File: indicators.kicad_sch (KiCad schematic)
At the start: 0 parts

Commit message: Added todo list
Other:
- note added: "TODO list: - RGB LED with PWM for status indication - LED indicators for each thing: (STM LED, 3.3V power LED, USB LED, SERVO LED, 12V LED, etc. - Add Buzzer too"
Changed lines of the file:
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@@
 	(generator_version "9.0")
 	(paper "A4")
+	(text "TODO list:\n- RGB LED with PWM for status indication\n- LED indicators for each thing: (STM LED, 3.3V power LED, USB LED, SERVO LED, 12V LED, etc.\n- Add Buzzer too"
+		(exclude_from_sim no)
+		(at 145.796 99.822 0)
+		(effects
+			(font
+				(size 2.54 2.54)
+				(thickness 0.508)
+				(bold yes)
+			)
+		)
+	)
 )

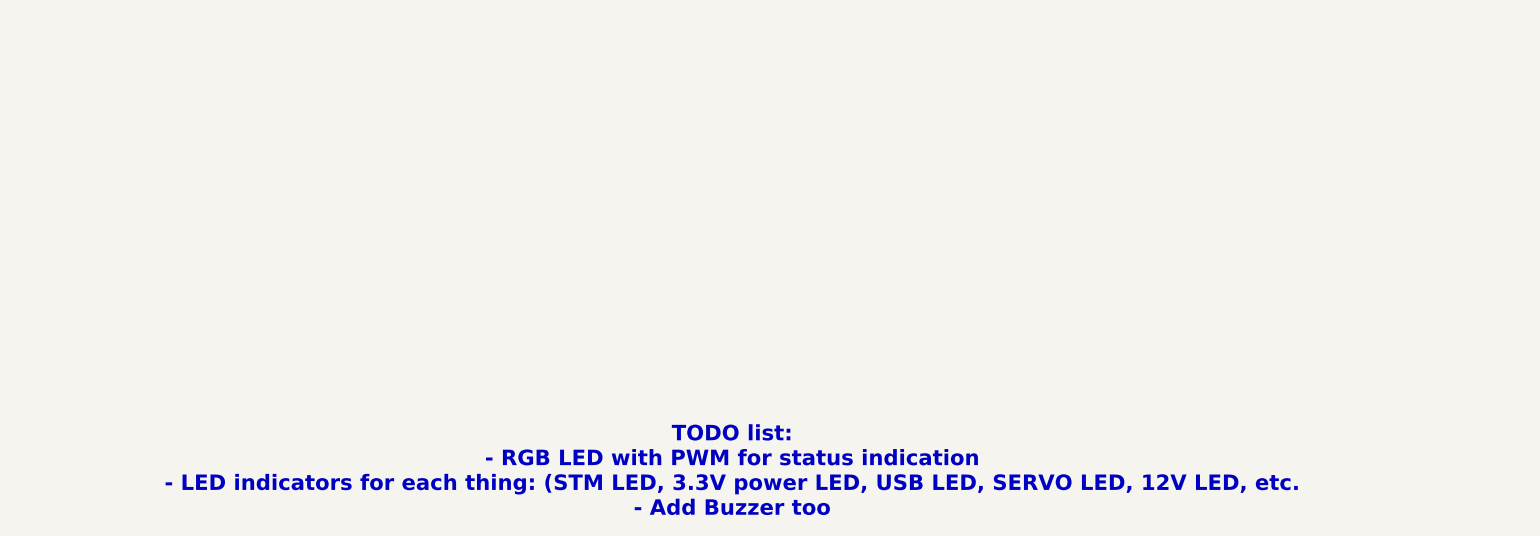
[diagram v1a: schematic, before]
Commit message: Added indicator circuits
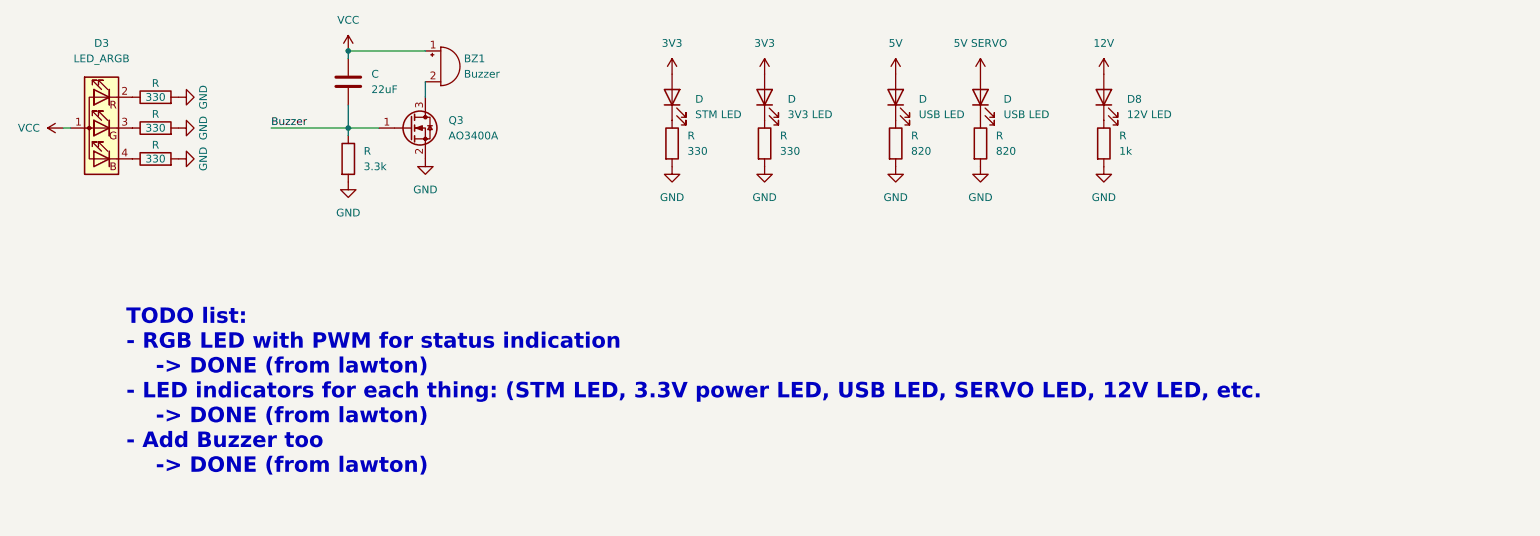
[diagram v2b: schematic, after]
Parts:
- added BZ1: Buzzer, symbol Device:Buzzer
- added C: 22uF, symbol Device:C
- added D: STM LED, symbol Device:LED
- added D (x2): USB LED, symbol Device:LED
- added D: 3V3 LED, symbol Device:LED
- added D3: LED_ARGB, symbol Device:LED_ARGB
- added D8: 12V LED, symbol Device:LED
- added Q3: AO3400A, Package_TO_SOT_SMD:SOT-23, symbol Transistor_FET:AO3400A
- added R: 3.3k, symbol Device:R
- added R (x5): 330, symbol Device:R
- added R (x2): 820, symbol Device:R
- added R: 1k, symbol Device:R
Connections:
- new net: D.1 (K), R.1 (x4)
- new net: D3.3 (GK), R.1
- new net: D8.1 (K), R.1
- new net: BZ1.2 (-), Q3.3 (D)
- new net: D3.4 (BK), R.1
- new net: D3.2 (RK), R.1
- new net 12V: D8.2 (A)
- new net 3V3: D.2 (A), D.2 (A)
- new net 5V: D.2 (A)
- new net 5V SERVO: D.2 (A)
- new net Buzzer: C.2, Q3.1 (G), R.1
- new net GND: Q3.2 (S), R.2, R.2, R.2, R.2, R.2, R.2, R.2, R.2, R.2
- new net VCC: BZ1.1 (+), C.1, D3.1 (A)
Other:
- note added: "TODO list: - RGB LED with PWM for status indication -> DONE (from lawton) - LED indicators for each thing: (STM LED, 3.3V power LED, USB LED, SERVO LED, 12V LED, etc. -> DONE (from lawton) - Add Buzzer too -> DONE (from lawton)"
- note removed: "TODO list: - RGB LED with PWM for status indication - LED indicators for each thing: (STM LED, 3.3V power LED, USB LED, SERVO LED, 12V LED, etc. - Add Buzzer too"
